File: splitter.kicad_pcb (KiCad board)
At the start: 2 copper layers, 40.6 x 65.4 mm, 7 parts, among them J1 NI68PinConnector, J2 NI68PinConnector, J3 PinHeaders

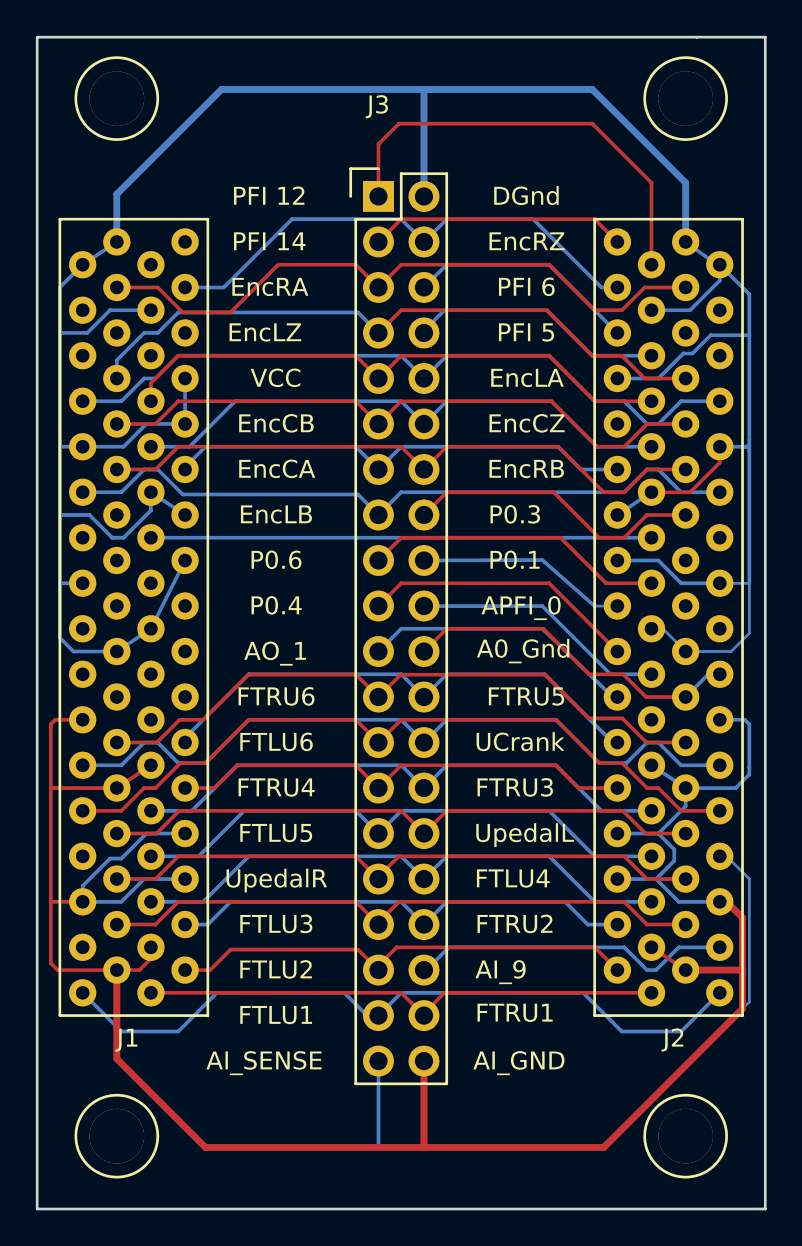
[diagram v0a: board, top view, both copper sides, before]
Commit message: updated standoff holes to be M3 clearance holes. Deleted stray traces that are located inside through holes, passed DRC.
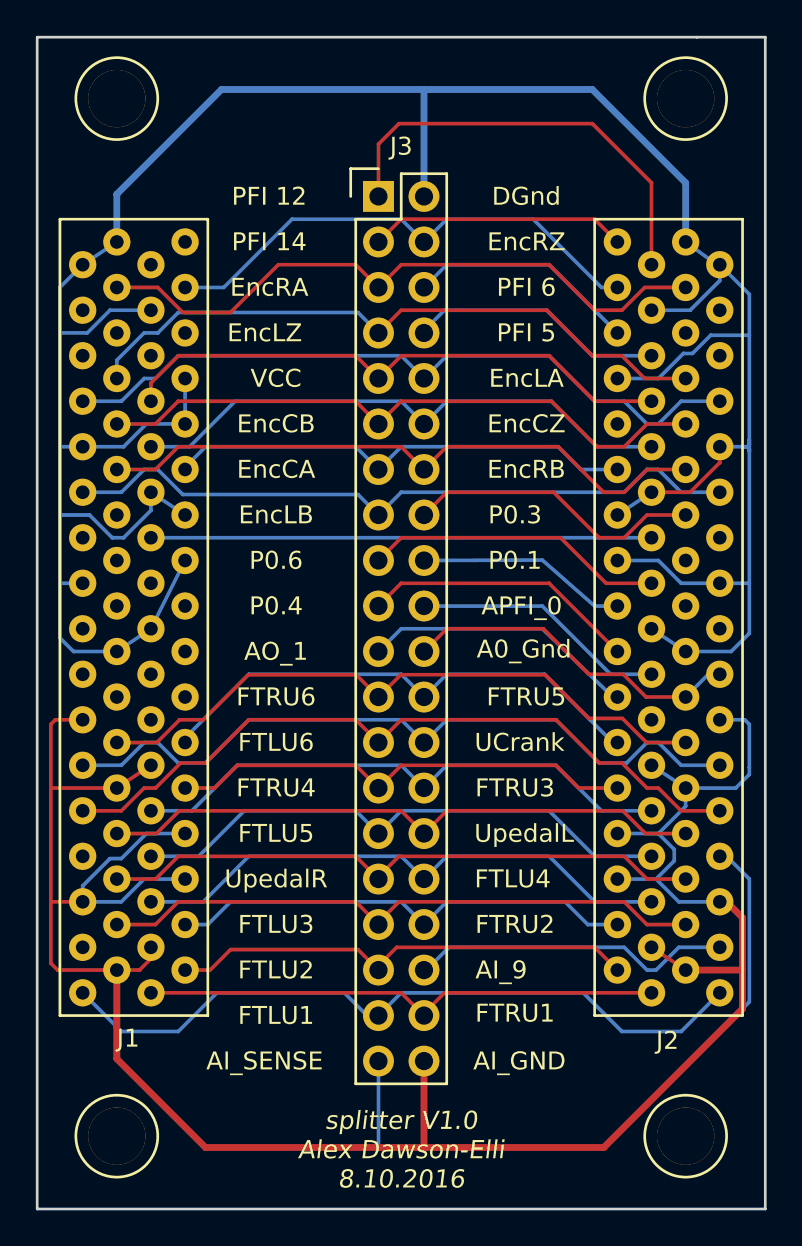
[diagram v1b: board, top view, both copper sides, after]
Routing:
- net /AO_Gnd: track 19.1 -> 18.5 mm
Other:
- net class Default: clearance 0.1524 -> 0.2032; trace_width 0.1524 -> 0.2032
- net class GND: clearance 0.1778 -> 0.2032
- rule trace_clearance: 0.1524 -> 0.2032
- rule trace_min: 0.1524 -> 0.2032
- board text added: "splitter V1.0 Alex Dawson-Elli 8.10.2016"
